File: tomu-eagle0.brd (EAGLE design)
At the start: 14 x 11.2 mm, 17 parts, among them U1 EFM32HG309F64G

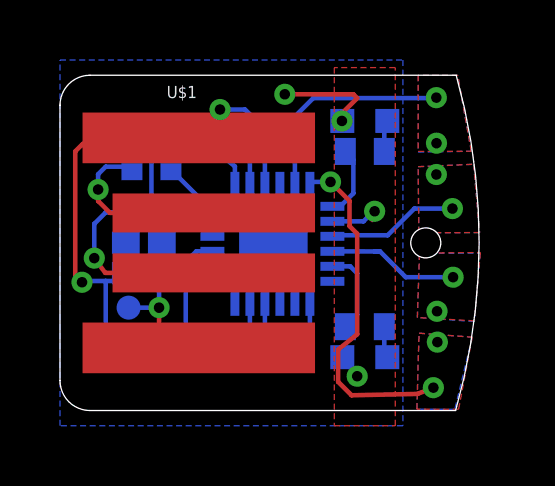
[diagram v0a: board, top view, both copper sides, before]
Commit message: sigh. QFN24 is 5x5 not 4x4
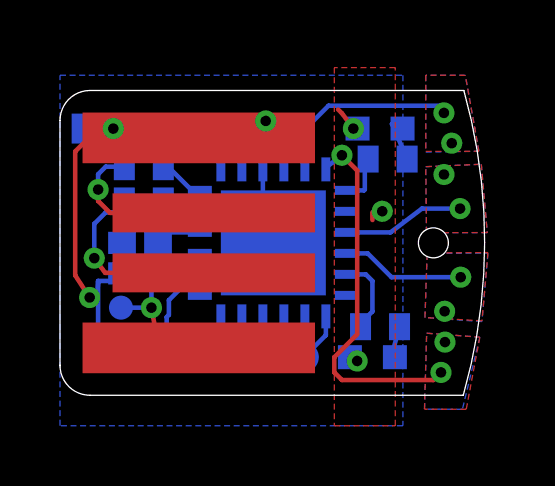
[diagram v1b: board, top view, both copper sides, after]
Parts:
- removed 5, RX, TX: TPTP08R, testpad:TP08R
- added -: TPTP10SQ, testpad:TP10SQ
- added 5V: TPTP08R, testpad:TP08R
- added RS, T: TPTP10R, testpad:TP10R
- C, D, R: value TPTP08R -> TPTP10R; device testpad:TP08R -> testpad:TP10R
- moved R 3.05 mm to (4.83, 2.03), turned to 0 degrees
- moved C 1.30 mm to (3.30, 9.65)
- moved R1 0.80 mm to (10.9, 8.64)
- moved C1 0.72 mm to (2.29, 2.54)
- moved LED2 0.57 mm to (10.7, 9.65)
- moved R2 0.51 mm to (10.7, 3.05)
- moved D 0.36 mm to (5.84, 9.65)
- moved R3 0.36 mm to (2.79, 7.24)
- moved R4 0.25 mm to (2.79, 8.38)
- moved LED1 0.25 mm to (10.4, 2.03)
- moved C2 0.13 mm to (2.67, 5.84)
- moved C3 0.13 mm to (2.67, 4.83)
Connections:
- net /RESET: now also RS.TP; no longer R.TP
- net GND: now also -.TP
- net LEUO_RX: now also R.TP; no longer RX.TP
- net LEUO_TX: now also T.TP; no longer TX.TP
- net VUSB: now also 5V.TP; no longer 5.TP
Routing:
- net +3V3: track 9.43 -> 3.95 mm, vias 4 -> 3
- net GND: track 22.1 -> 27.0 mm, vias 2 -> 3
- net CAP1B: track 11.5 -> 12.3 mm
- net LED1: track 2.39 -> 1.64 mm
- net CAP0B: track 7.23 -> 6.53 mm
- net DBG_SWCLK: track 2.19 -> 2.88 mm
- net RUSB_D+: track 2.41 -> 1.79 mm
- net N$5: track 1.06 -> 1.66 mm
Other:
- board size 14 x 11.2 mm -> 14.2 x 10.2 mm

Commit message: still dealing with QFN 4x4 -> 5x5 issues
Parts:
- moved R2 0.25 mm to (10.9, 3.05)
- moved C2 0.13 mm to (2.67, 5.97)
- moved C3 0.13 mm to (2.67, 4.95)
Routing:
- net +3V3: track 3.95 -> 6.88 mm
- net GND: track 27.0 -> 27.6 mm

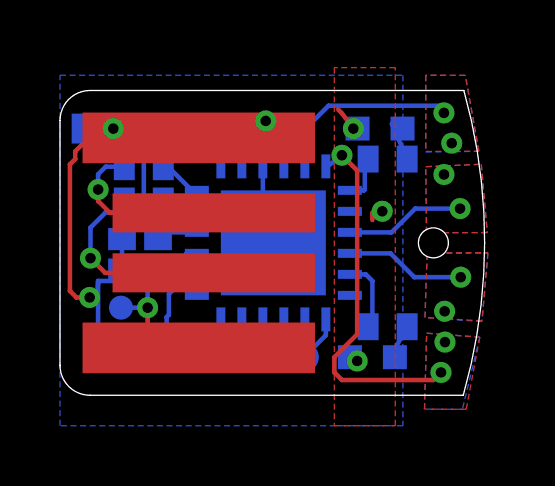
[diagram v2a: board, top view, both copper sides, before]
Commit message: fix CAP1A/CAP1B positions
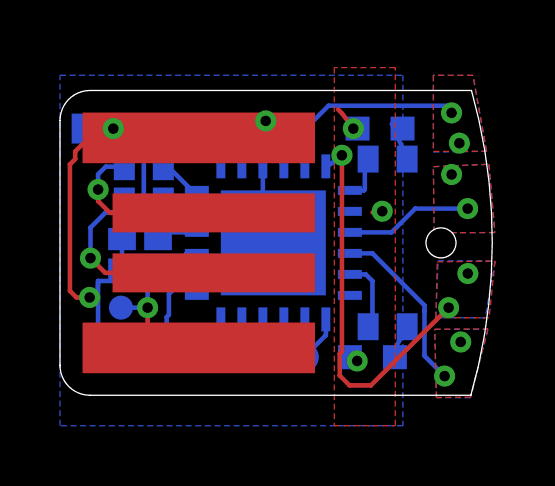
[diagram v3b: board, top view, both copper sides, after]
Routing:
- net CAP1A: track 4.02 -> 5.84 mm
- net CAP1B: track 12.2 -> 12.9 mm
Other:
- board size 14.2 x 10.2 mm -> 14.4 x 10.2 mm

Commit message: more fixes
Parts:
- 5V: value TPTP08R -> TPTP10R; device testpad:TP08R -> testpad:TP10R
- moved LED1 0.68 mm to (11.0, 2.29)
- moved LED2 0.46 mm to (11.0, 9.40)
- moved R2 0.28 mm to (11.0, 3.30)
- moved R1 0.28 mm to (11.0, 8.38)
- moved U$1 0.25 mm to (6.35, 5.84)
- moved D 0.18 mm to (5.97, 9.53)
- moved C 0.18 mm to (3.43, 9.53)
- moved R 0.13 mm to (4.83, 2.16)
- moved RS 0.13 mm to (8.13, 2.16)
- moved T 0.13 mm to (6.60, 2.16)
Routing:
- net GND: track 27.6 -> 25.6 mm
- net CAP1B: track 12.9 -> 14.6 mm
- net +3V3: track 6.88 -> 6.05 mm
- net N$5: track 1.66 -> 1.06 mm
- net CAP1A: track 5.84 -> 5.23 mm
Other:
- board size 14.4 x 10.2 mm -> 14.4 x 9.7 mm
- board text added: "tomu-eagle0"
